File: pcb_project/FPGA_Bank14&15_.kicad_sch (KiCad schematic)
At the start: 39 parts, among them IC3 IS61WV204816BLL-10TLI, IC4 IS61WV204816BLL-10TLI, U1 XC7A100T-FTG256, U9 MT25QL128ABA1ESE-0SIT

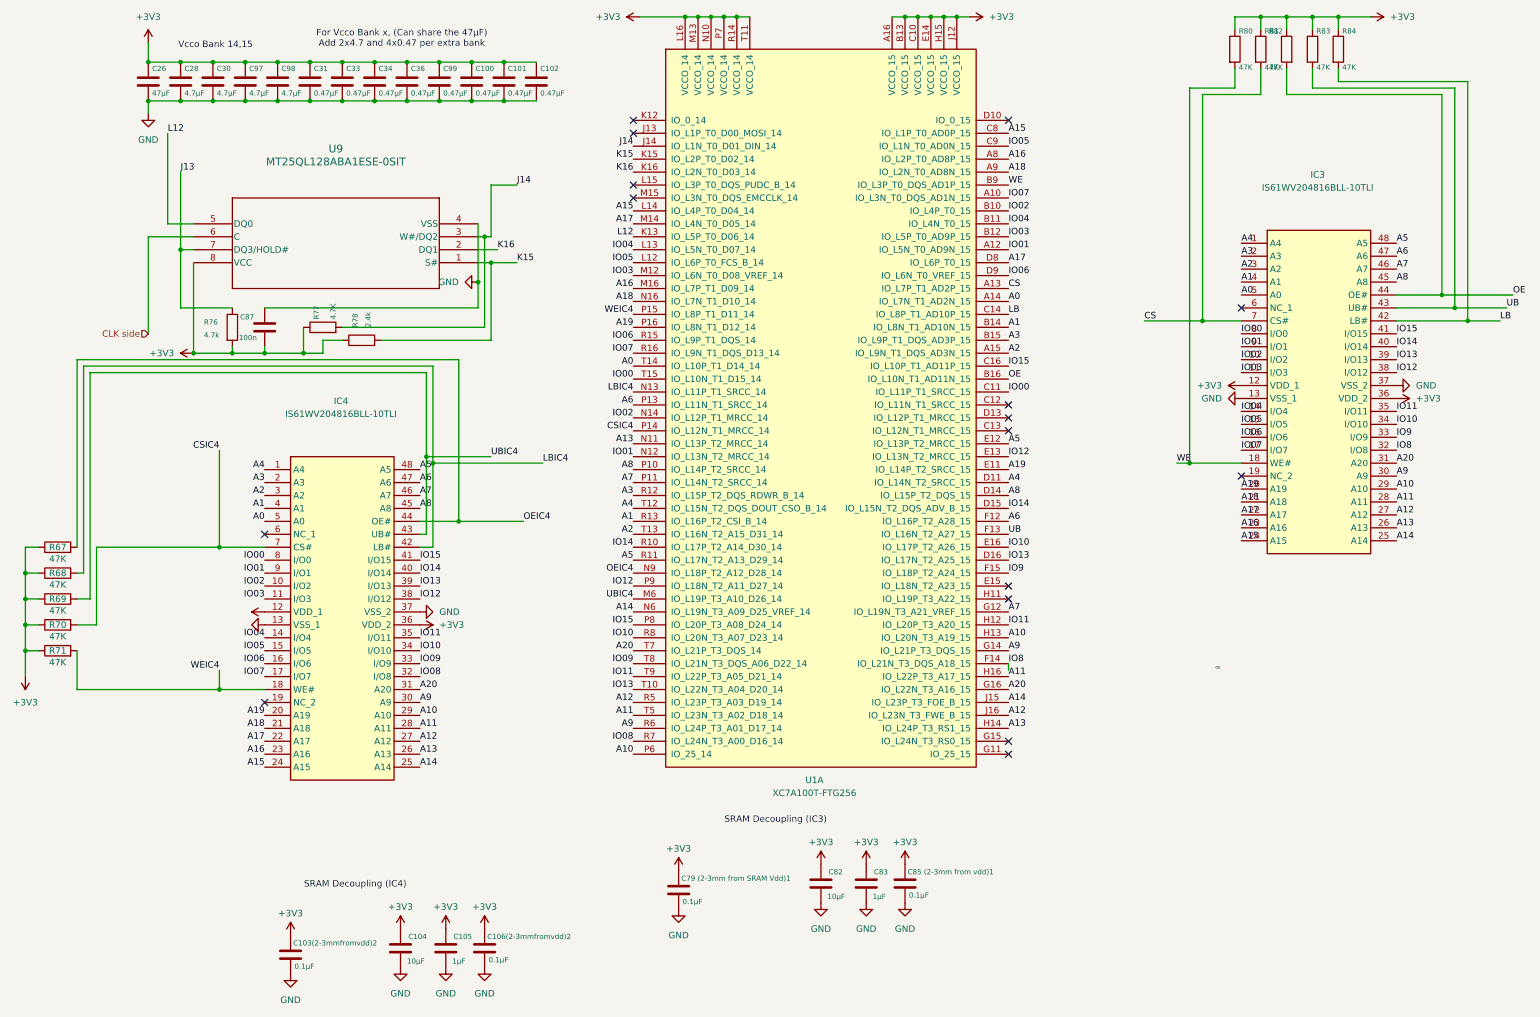
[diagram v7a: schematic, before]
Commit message: Connected wires for SRAMs
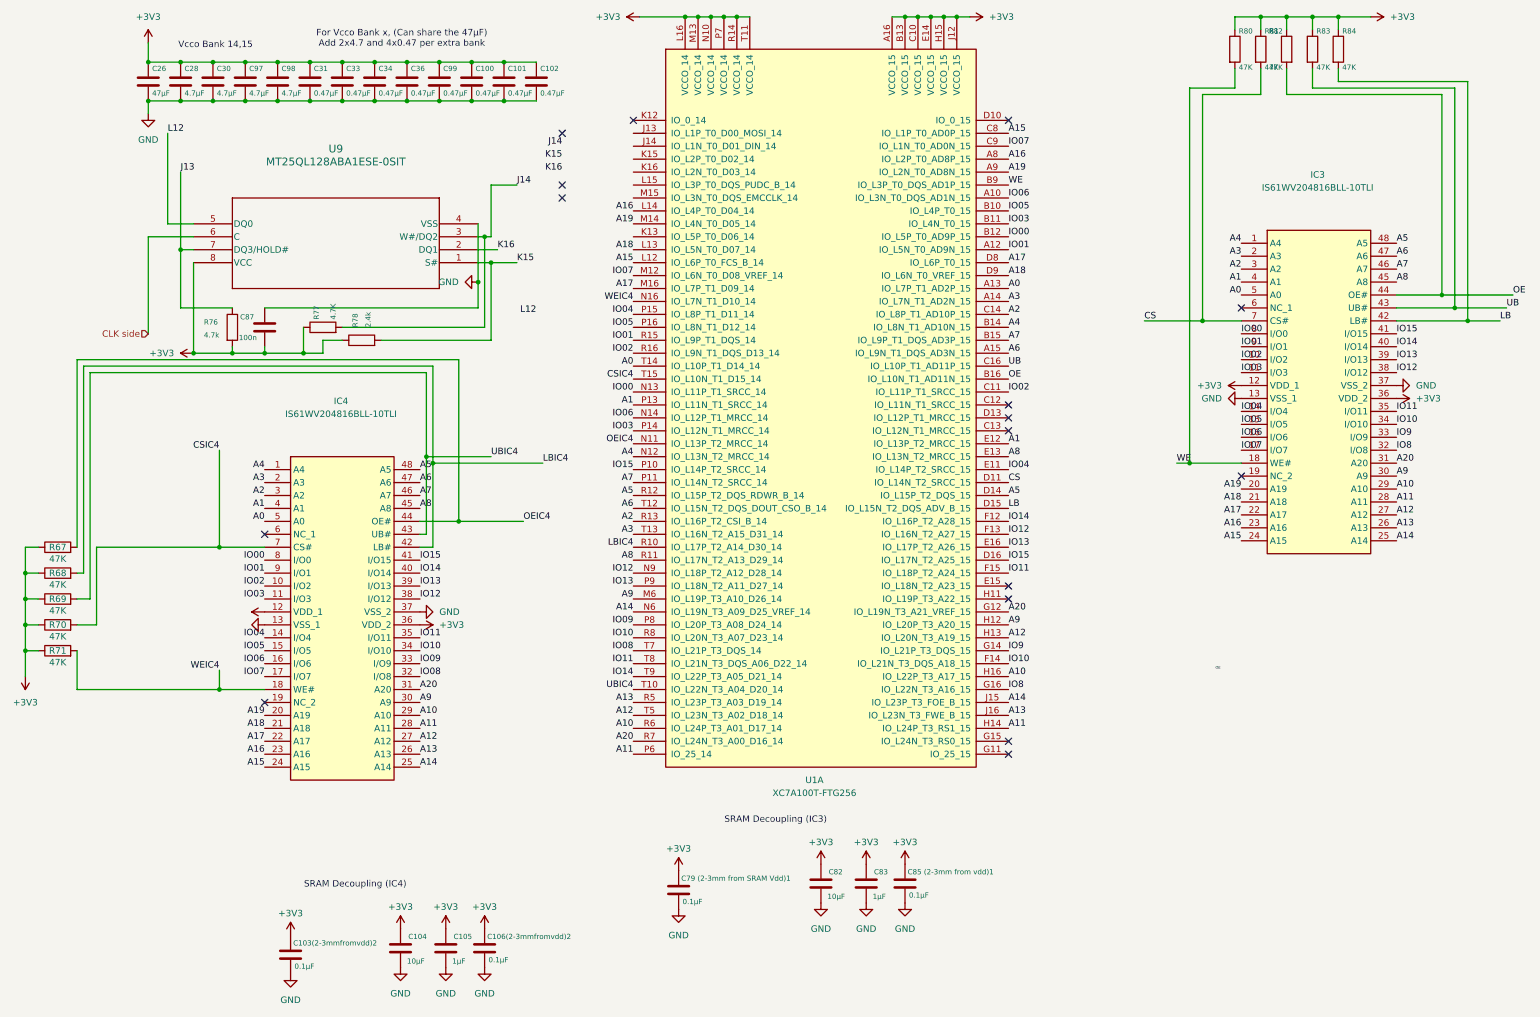
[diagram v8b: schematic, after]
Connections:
- net A0: now also U1.A13 (IO_L7P_T1_AD2P_15); no longer U1.A14 (IO_L7N_T1_AD2N_15)
- net A1: now also U1.E12 (IO_L13P_T2_MRCC_15), U1.P13 (IO_L11N_T1_SRCC_14); no longer U1.B14 (IO_L8N_T1_AD10N_15), U1.R13 (IO_L16P_T2_CSI_B_14)
- net A10: now also U1.H16 (IO_L22P_T3_A17_15), U1.R6 (IO_L24P_T3_A01_D17_14); no longer U1.H13 (IO_L20N_T3_A19_15), U1.P6 (IO_25_14)
- net A11: now also U1.H14 (IO_L24P_T3_RS1_15), U1.P6 (IO_25_14); no longer U1.H16 (IO_L22P_T3_A17_15), U1.T5 (IO_L23N_T3_A02_D18_14)
- net A12: now also U1.H13 (IO_L20N_T3_A19_15), U1.T5 (IO_L23N_T3_A02_D18_14); no longer U1.J16 (IO_L23N_T3_FWE_B_15), U1.R5 (IO_L23P_T3_A03_D19_14)
- net A13: now also U1.J16 (IO_L23N_T3_FWE_B_15), U1.R5 (IO_L23P_T3_A03_D19_14); no longer U1.H14 (IO_L24P_T3_RS1_15), U1.N11 (IO_L13P_T2_MRCC_14)
- net A15: now also U1.L12 (IO_L6P_T0_FCS_B_14); no longer U1.L14 (IO_L4P_T0_D04_14)
- net A16: now also U1.L14 (IO_L4P_T0_D04_14); no longer U1.M16 (IO_L7P_T1_D09_14)
- net A17: now also U1.M16 (IO_L7P_T1_D09_14); no longer U1.M14 (IO_L4N_T0_D05_14)
- net A18: now also U1.D9 (IO_L6N_T0_VREF_15), U1.L13 (IO_L5N_T0_D07_14); no longer U1.A9 (IO_L2N_T0_AD8N_15), U1.N16 (IO_L7N_T1_D10_14)
- net A19: now also U1.A9 (IO_L2N_T0_AD8N_15), U1.M14 (IO_L4N_T0_D05_14); no longer U1.E11 (IO_L14P_T2_SRCC_15), U1.P16 (IO_L8N_T1_D12_14)
- net A2: now also U1.C14 (IO_L8P_T1_AD10P_15), U1.R13 (IO_L16P_T2_CSI_B_14); no longer U1.A15 (IO_L9N_T1_DQS_AD3N_15), U1.T13 (IO_L16N_T2_A15_D31_14)
- net A20: now also U1.G12 (IO_L19N_T3_A21_VREF_15), U1.R7 (IO_L24N_T3_A00_D16_14); no longer U1.G16 (IO_L22N_T3_A16_15), U1.T7 (IO_L21P_T3_DQS_14)
- net A3: now also U1.A14 (IO_L7N_T1_AD2N_15), U1.T13 (IO_L16N_T2_A15_D31_14); no longer U1.B15 (IO_L9P_T1_DQS_AD3P_15), U1.R12 (IO_L15P_T2_DQS_RDWR_B_14)
- net A4: now also U1.B14 (IO_L8N_T1_AD10N_15), U1.N12 (IO_L13N_T2_MRCC_14); no longer U1.D11 (IO_L14N_T2_SRCC_15), U1.T12 (IO_L15N_T2_DQS_DOUT_CSO_B_14)
- net A5: now also U1.D14 (IO_L15P_T2_DQS_15), U1.R12 (IO_L15P_T2_DQS_RDWR_B_14); no longer U1.E12 (IO_L13P_T2_MRCC_15), U1.R11 (IO_L17N_T2_A13_D29_14)
- net A6: now also U1.A15 (IO_L9N_T1_DQS_AD3N_15), U1.T12 (IO_L15N_T2_DQS_DOUT_CSO_B_14); no longer U1.F12 (IO_L16P_T2_A28_15), U1.P13 (IO_L11N_T1_SRCC_14)
- net A7: now also U1.B15 (IO_L9P_T1_DQS_AD3P_15); no longer U1.G12 (IO_L19N_T3_A21_VREF_15)
- net A8: now also U1.E13 (IO_L13N_T2_MRCC_15), U1.R11 (IO_L17N_T2_A13_D29_14); no longer U1.D14 (IO_L15P_T2_DQS_15), U1.P10 (IO_L14P_T2_SRCC_14)
- net A9: now also U1.H12 (IO_L20P_T3_A20_15), U1.M6 (IO_L19P_T3_A10_D26_14); no longer U1.G14 (IO_L21P_T3_DQS_15), U1.R6 (IO_L24P_T3_A01_D17_14)
- net CS: now also U1.D11 (IO_L14N_T2_SRCC_15); no longer U1.A13 (IO_L7P_T1_AD2P_15)
- net CSIC4: now also U1.T15 (IO_L10N_T1_D15_14); no longer U1.P14 (IO_L12N_T1_MRCC_14)
- net IO00: now also U1.B12 (IO_L5P_T0_AD9P_15), U1.N13 (IO_L11P_T1_SRCC_14); no longer U1.C11 (IO_L11P_T1_SRCC_15), U1.T15 (IO_L10N_T1_D15_14)
- net IO01: now also U1.R15 (IO_L9P_T1_DQS_14); no longer U1.N12 (IO_L13N_T2_MRCC_14)
- net IO02: now also U1.C11 (IO_L11P_T1_SRCC_15), U1.R16 (IO_L9N_T1_DQS_D13_14); no longer U1.B10 (IO_L4P_T0_15), U1.N14 (IO_L12P_T1_MRCC_14)
- net IO03: now also U1.B11 (IO_L4N_T0_15), U1.P14 (IO_L12N_T1_MRCC_14); no longer U1.B12 (IO_L5P_T0_AD9P_15), U1.M12 (IO_L6N_T0_D08_VREF_14)
- net IO04: now also U1.E11 (IO_L14P_T2_SRCC_15), U1.P15 (IO_L8P_T1_D11_14); no longer U1.B11 (IO_L4N_T0_15), U1.L13 (IO_L5N_T0_D07_14)
- net IO05: now also U1.B10 (IO_L4P_T0_15), U1.P16 (IO_L8N_T1_D12_14); no longer U1.C9 (IO_L1N_T0_AD0N_15), U1.L12 (IO_L6P_T0_FCS_B_14)
- net IO06: now also U1.A10 (IO_L3N_T0_DQS_AD1N_15), U1.N14 (IO_L12P_T1_MRCC_14); no longer U1.D9 (IO_L6N_T0_VREF_15), U1.R15 (IO_L9P_T1_DQS_14)
- net IO07: now also U1.C9 (IO_L1N_T0_AD0N_15), U1.M12 (IO_L6N_T0_D08_VREF_14); no longer U1.A10 (IO_L3N_T0_DQS_AD1N_15), U1.R16 (IO_L9N_T1_DQS_D13_14)
- net IO08: now also U1.T7 (IO_L21P_T3_DQS_14); no longer U1.R7 (IO_L24N_T3_A00_D16_14)
- net IO09: now also U1.P8 (IO_L20P_T3_A08_D24_14); no longer U1.T8 (IO_L21N_T3_DQS_A06_D22_14)
- net IO10: now also U1.F14 (IO_L21N_T3_DQS_A18_15); no longer U1.E16 (IO_L17P_T2_A26_15)
- net IO11: now also U1.F15 (IO_L18P_T2_A24_15), U1.T8 (IO_L21N_T3_DQS_A06_D22_14); no longer U1.H12 (IO_L20P_T3_A20_15), U1.T9 (IO_L22P_T3_A05_D21_14)
- net IO12: now also U1.F13 (IO_L16N_T2_A27_15), U1.N9 (IO_L18P_T2_A12_D28_14); no longer U1.E13 (IO_L13N_T2_MRCC_15), U1.P9 (IO_L18N_T2_A11_D27_14)
- net IO13: now also U1.E16 (IO_L17P_T2_A26_15), U1.P9 (IO_L18N_T2_A11_D27_14); no longer U1.D16 (IO_L17N_T2_A25_15), U1.T10 (IO_L22N_T3_A04_D20_14)
- net IO14: now also U1.F12 (IO_L16P_T2_A28_15), U1.T9 (IO_L22P_T3_A05_D21_14); no longer U1.D15 (IO_L15N_T2_DQS_ADV_B_15), U1.R10 (IO_L17P_T2_A14_D30_14)
- net IO15: now also U1.D16 (IO_L17N_T2_A25_15), U1.P10 (IO_L14P_T2_SRCC_14); no longer U1.C16 (IO_L10P_T1_AD11P_15), U1.P8 (IO_L20P_T3_A08_D24_14)
- net IO8: now also U1.G16 (IO_L22N_T3_A16_15); no longer U1.F14 (IO_L21N_T3_DQS_A18_15)
- net IO9: now also U1.G14 (IO_L21P_T3_DQS_15); no longer U1.F15 (IO_L18P_T2_A24_15)
- net J14: no longer U1.J14 (IO_L1N_T0_D01_DIN_14)
- net K15: no longer U1.K15 (IO_L2P_T0_D02_14)
- net K16: no longer U1.K16 (IO_L2N_T0_D03_14)
- net L12: no longer U1.K13 (IO_L5P_T0_D06_14)
- net LB: now also U1.D15 (IO_L15N_T2_DQS_ADV_B_15); no longer U1.C14 (IO_L8P_T1_AD10P_15)
- net LBIC4: now also U1.R10 (IO_L17P_T2_A14_D30_14); no longer U1.N13 (IO_L11P_T1_SRCC_14)
- net OEIC4: now also U1.N11 (IO_L13P_T2_MRCC_14); no longer U1.N9 (IO_L18P_T2_A12_D28_14)
- net UB: now also U1.C16 (IO_L10P_T1_AD11P_15); no longer U1.F13 (IO_L16N_T2_A27_15)
- net UBIC4: now also U1.T10 (IO_L22N_T3_A04_D20_14); no longer U1.M6 (IO_L19P_T3_A10_D26_14)
- net WEIC4: now also U1.N16 (IO_L7N_T1_D10_14); no longer U1.P15 (IO_L8P_T1_D11_14)
